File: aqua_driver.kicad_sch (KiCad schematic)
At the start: 9 parts, among them J1 HEATER IN, J2 230V IN, K1 FINDER-36.11, Q1 2N7000, U1 TCMT1100

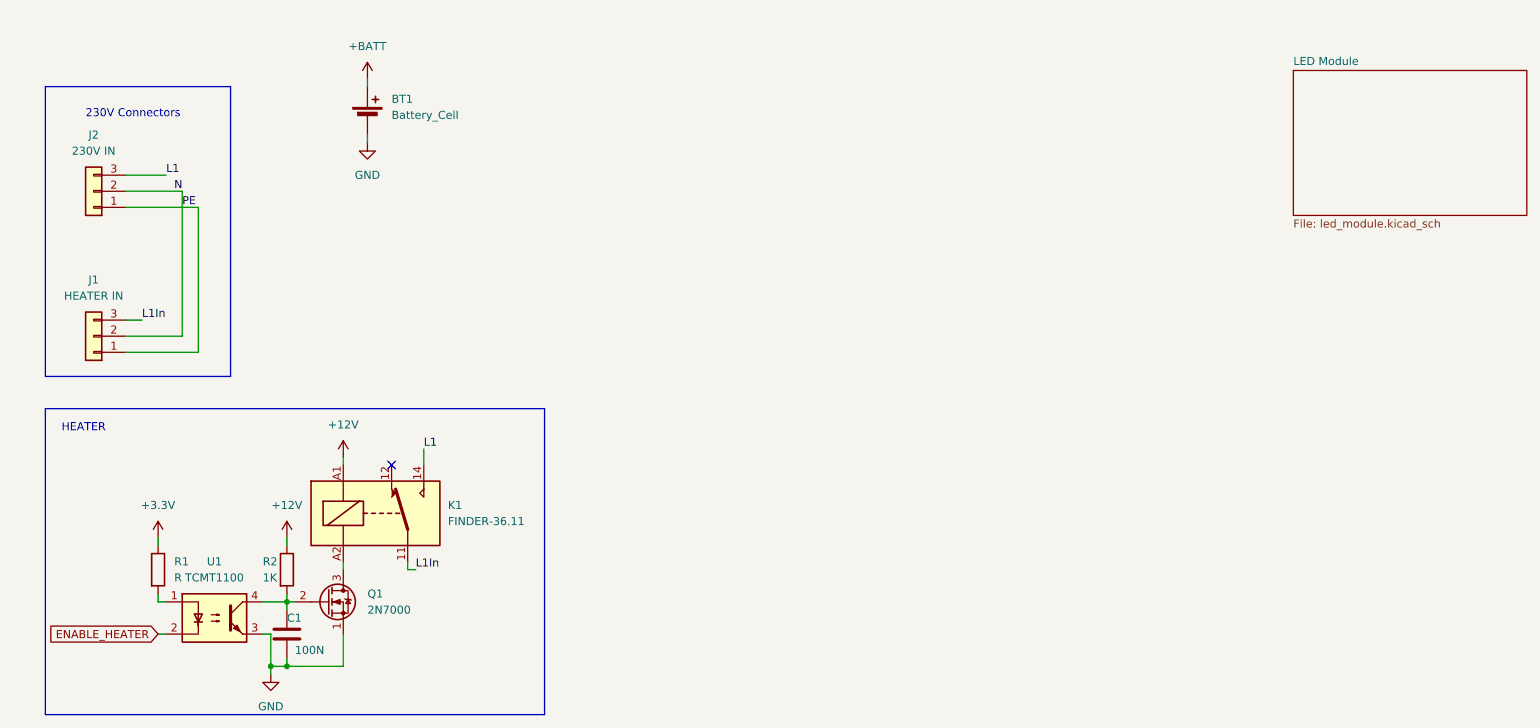
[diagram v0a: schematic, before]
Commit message: Basic work (#4)
* Added/Updated KiCAD project files.
Added 230V connectors to schematic.
Added basic relay circuit to schematic.
Added .gitignore file.

* Fixed floating point in config.

* Working on aqua_driver - temperature sensors.

* Added main subsheets for led, power and temperature control.

* Fixed merge.

* Working on aqua_driver - temperature sensors.

* Fixed project file.

---------

Co-authored-by: Sławomir Kozok <slawomir.kozok@3dgence.com>
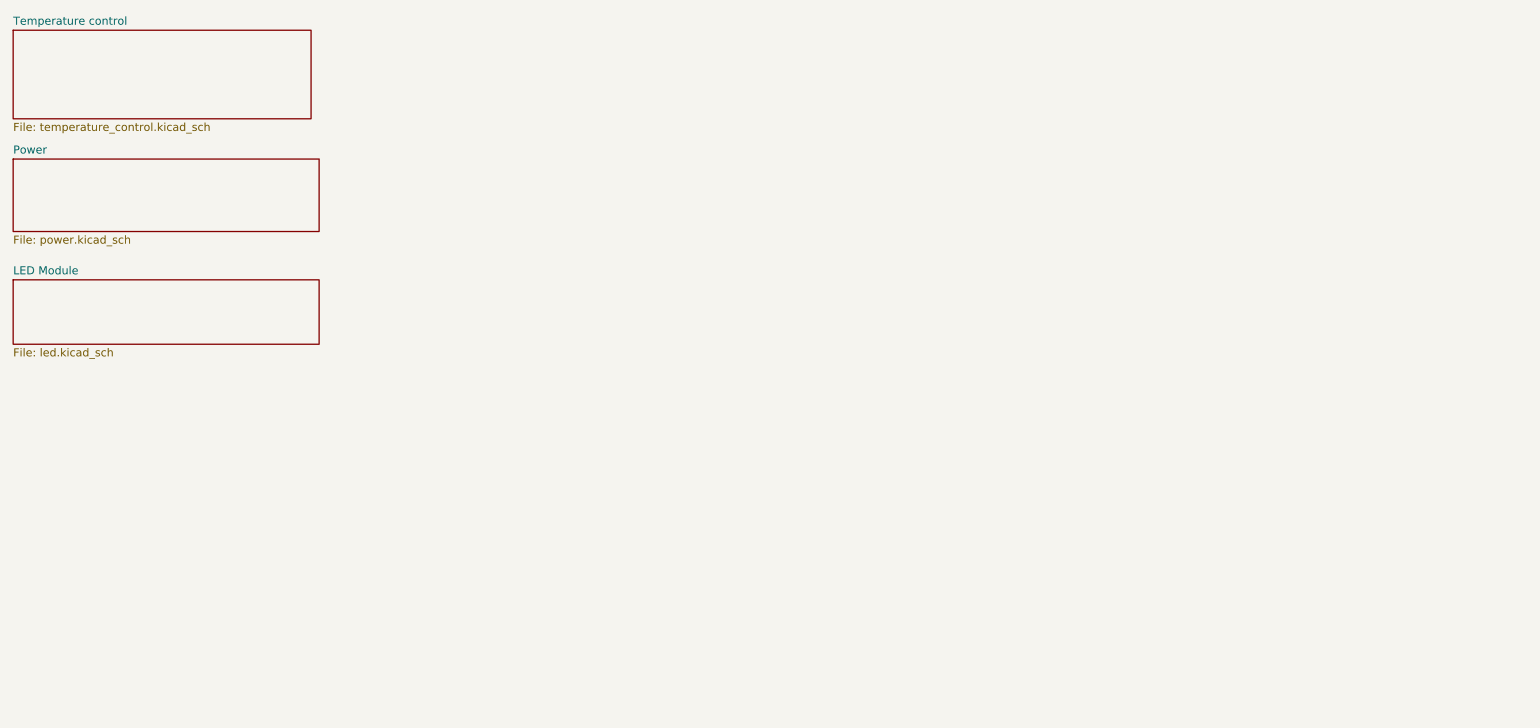
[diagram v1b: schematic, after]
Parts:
- removed BT1: Battery_Cell, symbol Device:Battery_Cell
- removed C1: 100N, symbol Device:C
- removed J1: HEATER IN, symbol Connector_Generic:Conn_01x03
- removed J2: 230V IN, symbol Connector_Generic:Conn_01x03
- removed K1: FINDER-36.11, Relay_THT:Relay_SPDT_Finder_36.11, symbol Relay:FINDER-36.11
- removed Q1: 2N7000, Package_TO_SOT_THT:TO-92_Inline, symbol Transistor_FET:2N7000
- removed R1: R, symbol Device:R
- removed R2: 1K, symbol Device:R
- removed U1: TCMT1100, Package_SO:SOP-4_4.4x2.6mm_P1.27mm, symbol Isolator:TCMT1100
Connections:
- no-connect marks 1 -> 0
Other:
- added sheet Power (power.kicad_sch)
- added sheet Temperature control (temperature_control.kicad_sch)
- sheet LED Module: file led_module.kicad_sch -> led.kicad_sch
- note removed: "230V Connectors"
- note removed: "HEATER"
- title: (none) -> Aqua Driver

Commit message: Add bluetooth sheet
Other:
- added sheet Bluetooth module (bluetooth_module.kicad_sch)
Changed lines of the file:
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@@
+    )
+  )
+  (sheet (at 25.4 83.82) (size 46.99 11.43) (fields_autoplaced)
+    (stroke (width 0.1524) (type solid))
+    (fill (color 0 0 0 0.0000))
+    (property "Sheetname" "Bluetooth module" (at 25.4 83.1084 0)
+      (effects (font (size 1.27 1.27)) (justify left bottom))
+    )
+    (property "Sheetfile" "bluetooth_module.kicad_sch" (at 25.4 95.8346 0)
+      (effects (font (size 1.27 1.27)) (justify left top))
+    )
+    (instances
+      (project "aqua_driver"
+        (path "/13f34ed6-0d14-48e4-b5f6-041bf4b3feac" (page "5"))
+      )
     )
   )

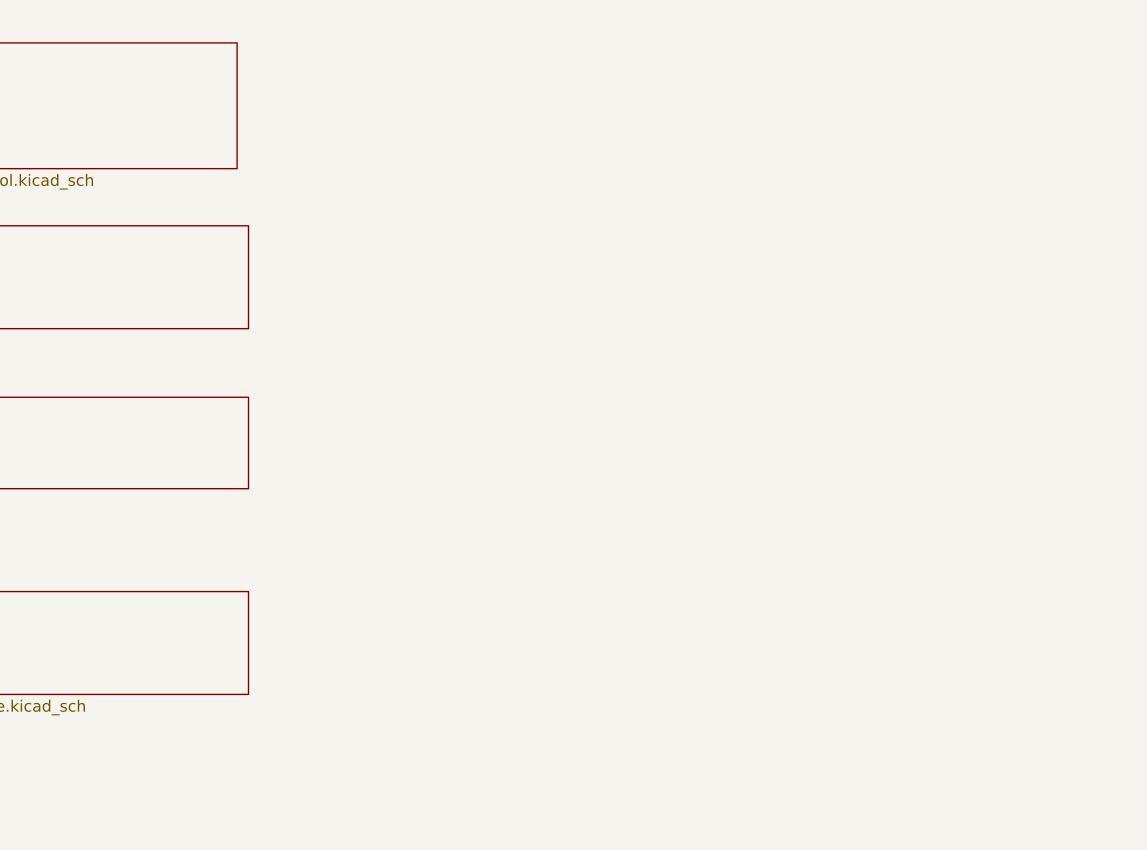
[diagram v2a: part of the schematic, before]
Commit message: Place uC with basic connectivity with bluetooth
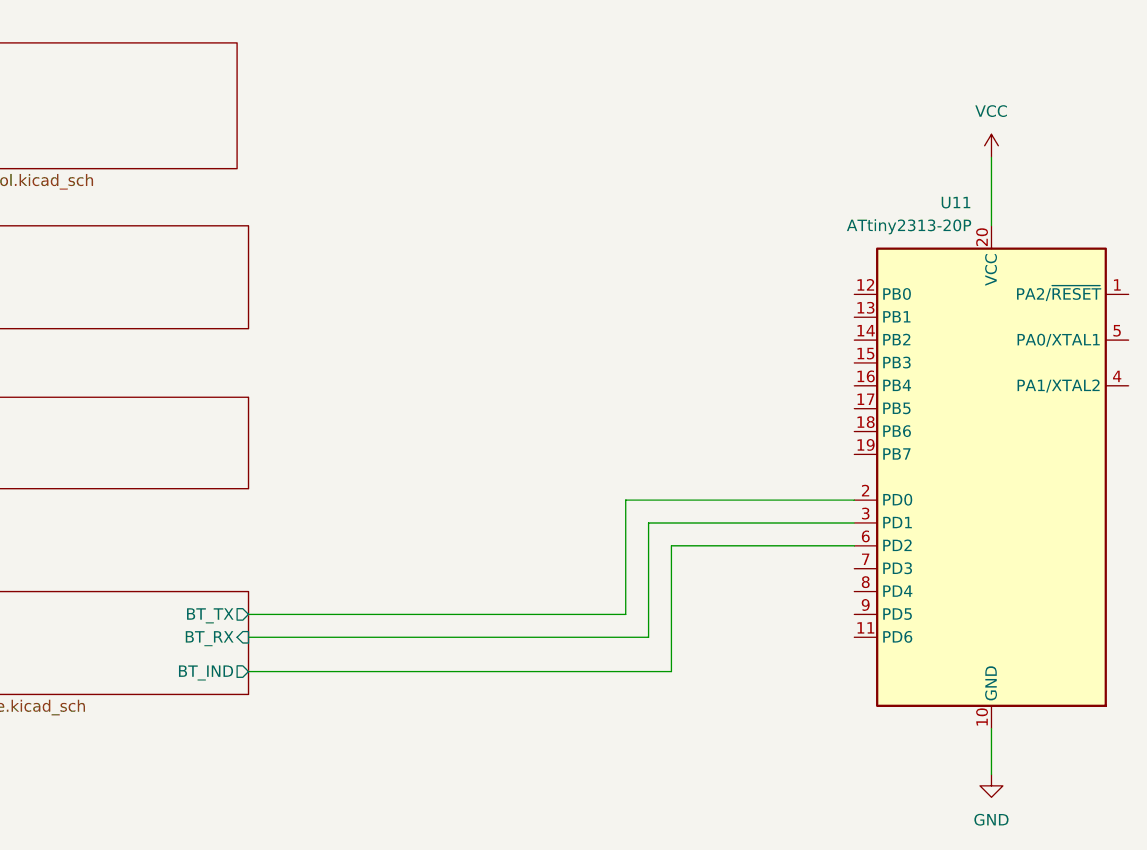
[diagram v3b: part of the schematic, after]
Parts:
- added U11: ATtiny2313-20P, Package_DIP:DIP-20_W7.62mm, symbol MCU_Microchip_ATtiny:ATtiny2313-20P
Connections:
- new net Bluetooth module/BT_IND: U11.6 (PD2)
- new net Bluetooth module/BT_RX: U11.3 (PD1)
- new net Bluetooth module/BT_TX: U11.2 (PD0)
- new net GND: U11.10 (GND)
- new net VCC: U11.20 (VCC)
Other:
- sheet Bluetooth module ports: added BT_IND, BT_RX, BT_TX; removed none
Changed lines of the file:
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@@
     (comment 3 "2023")
+  )
+  (wire (pts (xy 72.39 86.36) (xy 114.3 86.36))
+    (stroke (width 0) (type default))
+  )
+  (wire (pts (xy 114.3 86.36) (xy 114.3 73.66))
+    (stroke (width 0) (type default))
+  )
+  (wire (pts (xy 114.3 73.66) (xy 139.7 73.66))
+    (stroke (width 0) (type default))
+  )
+  (wire (pts (xy 119.38 92.71) (xy 119.38 78.74))
+    (stroke (width 0) (type default))
+  )
+  (wire (pts (xy 154.94 99.06) (xy 154.94 104.14))
+    (stroke (width 0) (type default))
+  )
+  (wire (pts (xy 116.84 88.9) (xy 72.39 88.9))
+    (stroke (width 0) (type default))
+  )
+  (wire (pts (xy 139.7 76.2) (xy 116.84 76.2))
+    (stroke (width 0) (type default))
+  )
+  (wire (pts (xy 154.94 35.56) (xy 154.94 43.18))
+    (stroke (width 0) (type default))
+  )
+  (wire (pts (xy 72.39 92.71) (xy 119.38 92.71))
+    (stroke (width 0) (type default))
+  )
+  (wire (pts (xy 119.38 78.74) (xy 139.7 78.74))
+    (stroke (width 0) (type default))
+  )
+  (wire (pts (xy 116.84 76.2) (xy 116.84 88.9))
+    (stroke (width 0) (type default))
+  )
+  (symbol (lib_id "power:VCC") (at 154.94 35.56 0) (unit 1)
+    (in_bom yes) (on_board yes) (dnp no) (fields_autoplaced)
+    (property "Reference" "#PWR024" (at 154.94 39.37 0)
+      (effects (font (size 1.27 1.27)) hide)
+    )
+    (property "Value" "VCC" (at 154.94 30.48 0)
+      (effects (font (size 1.27 1.27)))
+    )
+    (property "Footprint" "" (at 154.94 35.56 0)
+      (effects (font (size 1.27 1.27)) hide)
+    )
+    (property "Datasheet" "" (at 154.94 35.56 0)
+      (effects (font (size 1.27 1.27)) hide)
+    )
+    (pin "1")
+    (instances
+      (project "aqua_driver"
+        (path "/13f34ed6-0d14-48e4-b5f6-041bf4b3feac"
+          (reference "#PWR024") (unit 1)
+        )
+      )
+    )
+  )
+  (symbol (lib_id "power:GND") (at 154.94 104.14 0) (unit 1)
+    (in_bom yes) (on_board yes) (dnp no) (fields_autoplaced)
+    (property "Reference" "#PWR02" (at 154.94 110.49 0)
+      (effects (font (size 1.27 1.27)) hide)
+    )
+    (property "Value" "GND" (at 154.94 109.22 0)
+      (effects (font (size 1.27 1.27)))
+    )
+    (property "Footprint" "" (at 154.94 104.14 0)
+      (effects (font (size 1.27 1.27)) hide)
+    )
+    (property "Datasheet" "" (at 154.94 104.14 0)
+      (effects (font (size 1.27 1.27)) hide)
+    )
+    (pin "1")
+    (instances
+      (project "aqua_driver"
+        (path "/13f34ed6-0d14-48e4-b5f6-041bf4b3feac"
+          (reference "#PWR02") (unit 1)
+        )
+      )
+    )
+  )
+  (symbol (lib_id "MCU_Microchip_ATtiny:ATtiny2313-20P") (at 154.94 71.12 0) (mirror y) (unit 1)
+    (in_bom yes) (on_board yes) (dnp no)
+    (property "Reference" "U11" (at 152.7459 40.64 0)
+      (effects (font (size 1.27 1.27)) (justify left))
+    )
+    (property "Value" "ATtiny2313-20P" (at 152.7459 43.18 0)
+      (effects (font (size 1.27 1.27)) (justify left))
+    )
+    (property "Footprint" "Package_DIP:DIP-20_W7.62mm" (at 154.94 71.12 0)
+      (effects (font (size 1.27 1.27) italic) hide)
+    )
+    (property "Datasheet" "http://ww1.microchip.com/downloads/en/DeviceDoc/Atmel-2543-AVR-ATtiny2313_Datasheet.pdf" (at 154.94 71.12 0)
+      (effects (font (size 1.27 1.27)) hide)
+    )
+    (pin "16")
+    (pin "7")
+    (pin "6")
+    (pin "20")
+    (pin "13")
+    (pin "15")
+    (pin "2")
+    (pin "14")
+    (pin "3")
+    (pin "5")
+    (pin "11")
+    (pin "9")
+    (pin "12")
+    (pin "10")
+    (pin "17")
+    (pin "8")
+    (pin "1")
+    (pin "19")
+    (pin "18")
+    (pin "4")
+    (instances
+      (project "aqua_driver"
+        (path "/13f34ed6-0d14-48e4-b5f6-041bf4b3feac"
+          (reference "U11") (unit 1)
+        )
+      )
+    )
   )
   (sheet (at 24.13 22.86) (size 46.99 13.97) (fields_autoplaced)
@@
       (effects (font (size 1.27 1.27)) (justify left top))
     )
+    (pin "BT_RX" input (at 72.39 88.9 0)
+      (effects (font (size 1.27 1.27)) (justify right))
+    )
+    (pin "BT_TX" output (at 72.39 86.36 0)
+      (effects (font (size 1.27 1.27)) (justify right))
+    )
+    (pin "BT_IND" output (at 72.39 92.71 0)
+      (effects (font (size 1.27 1.27)) (justify right))
+    )
     (instances
